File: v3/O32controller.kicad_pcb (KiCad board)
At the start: 4 copper layers, 27 x 27 mm, 125 parts, among them J1 BATT+, J10 Motor Connection, J11 Motor Connection, J12 Motor Connection, J2 BATT+, J3 BATT-, J4 BATT-, J5 NTC, J6 SWD, J7 ExternalSPI, J8 RS485, J9 RS485, Q1 CSD88584Q5DC, Q2 CSD88584Q5DC, Q3 CSD88584Q5DC, U1 STSPIN32F0ATR, U2 THVD1420DRLR, U3 MA702GQ-P

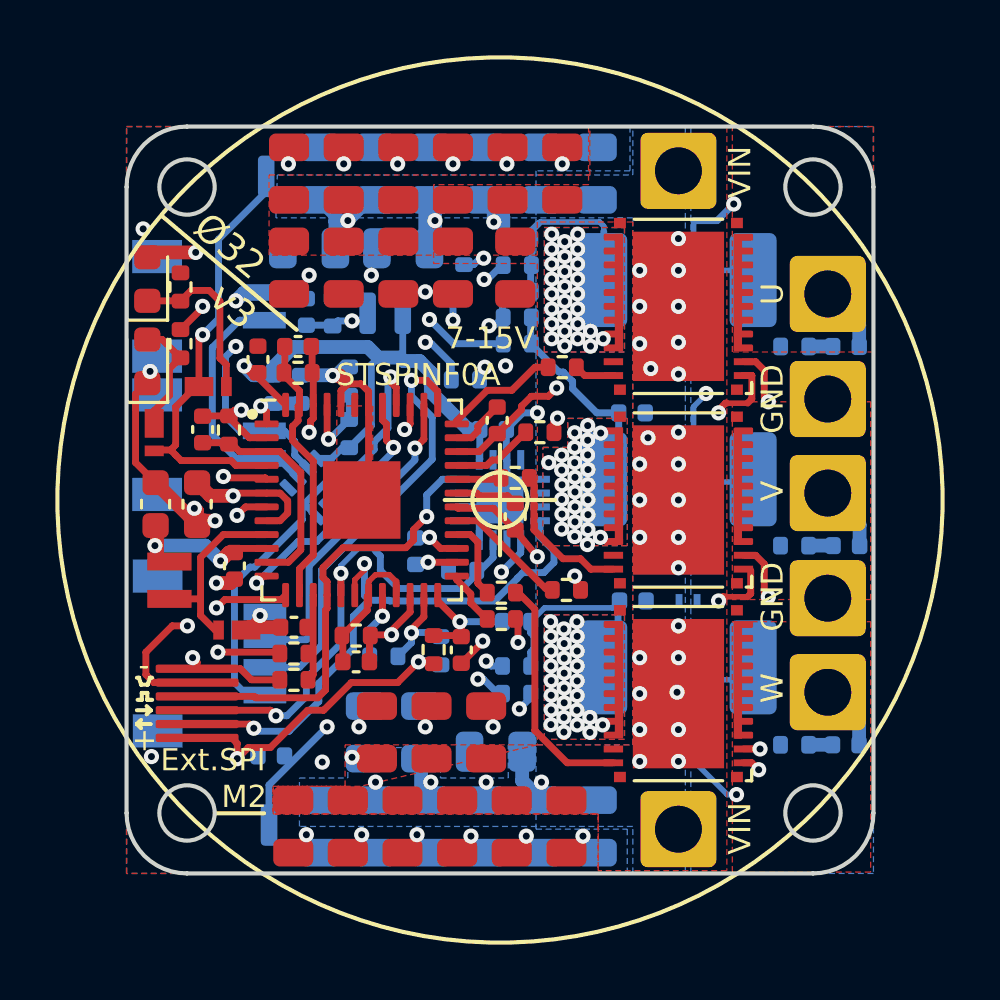
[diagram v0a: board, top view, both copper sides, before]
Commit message: use MA732 instead of 702, SMF15A
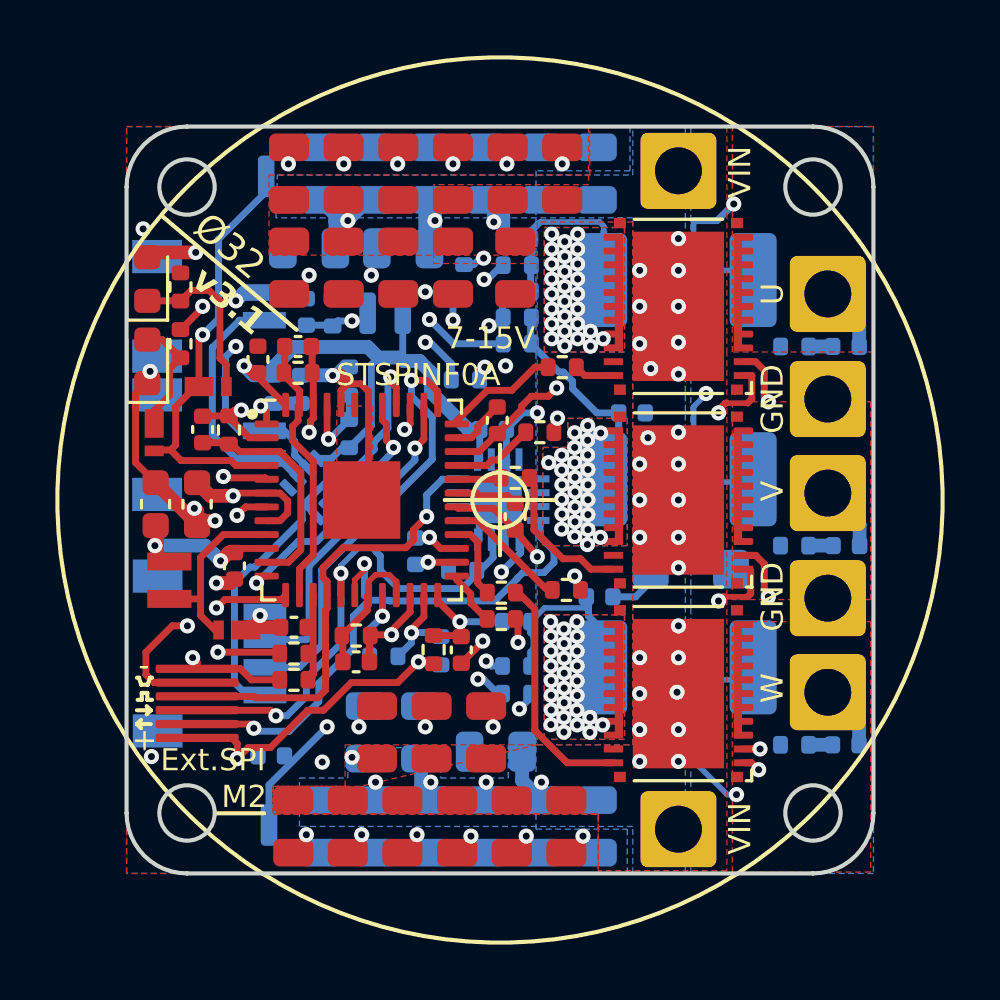
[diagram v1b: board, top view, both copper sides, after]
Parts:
- removed D2: ESDA17P20-1F2, O32controller:SMT2_0P91X0P63_STM-L
- added D7: SMF15A, Diode_SMD:D_SMF, B.Cu at (56.9, 52.5)
- U3: value MA702GQ-P -> MA732GQ-Z; footprint O32controller:MA702GQ-P -> O32controller:QFN-16_MA732
- moved C18 1.21 mm to (53.6, 53.5)
- moved U3 0.06 mm to (49.9, 50.0)
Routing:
- net VBUS: track 42.0 -> 44.1 mm
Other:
- board text added: "[07/29/24]"
- board text added: "v3.1"
- board text removed: "[12/27/23]"
- board text removed: "v3"

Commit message: finalize BOM for v3.1, shared w Axlab
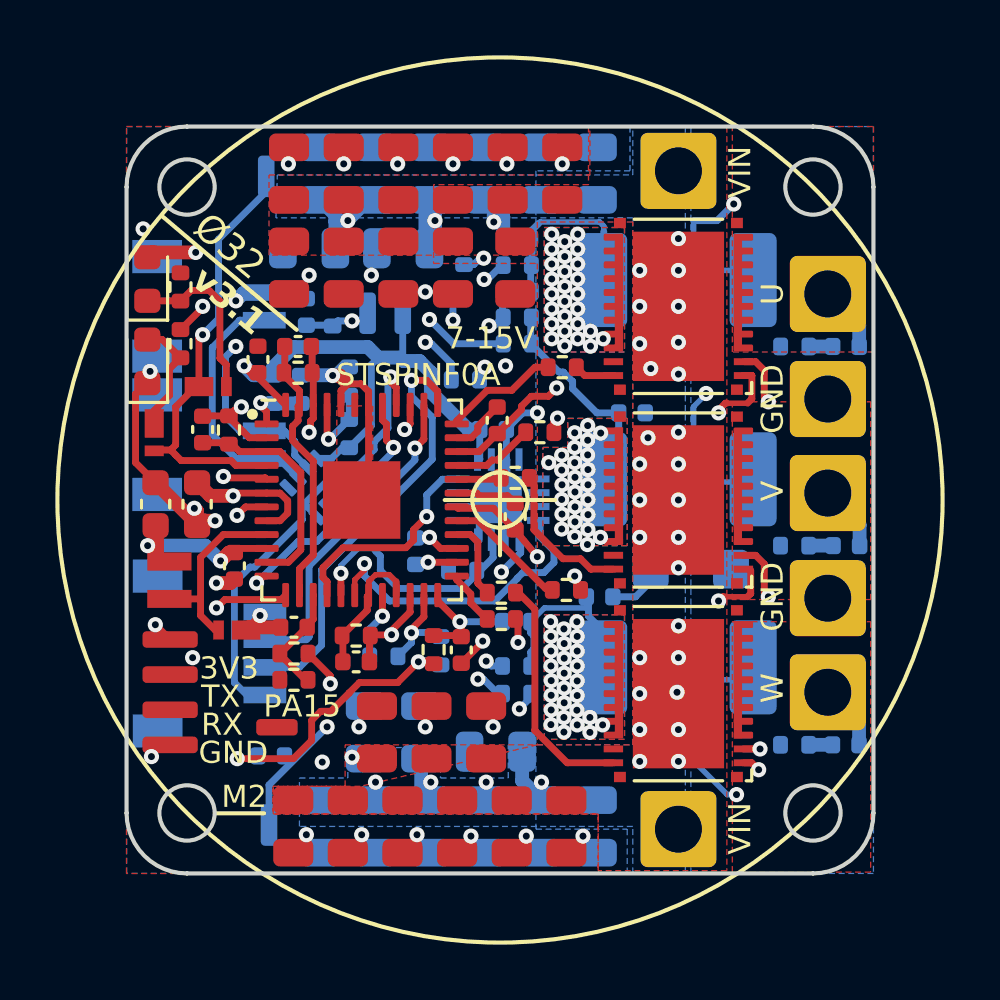
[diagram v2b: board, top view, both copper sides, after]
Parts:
- added J13: PA15, O32controller:SolderPad1-1.27mm, F.Cu at (41.9, 58.2)
- J7: value ExternalSPI -> AuxUART; footprint O32controller:FFC_0.5mm_6p -> O32controller:SolderUART-1.27mm
- moved J7 1.44 mm to (38.1, 55.0)
- turned R8 to 180 degrees
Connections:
- J7 pad 1: GND -> +3.3V
- J7 pad 2: /~{MAG2_CS} -> USART_TX
- J7 pad 3: /SPI_SCLK -> /USART_RX
- J7 pad 4: /SPI_MISO -> GND
- U1 pad 39: /~{MAG2_CS} -> /PA15
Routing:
- net /PA15: track 0.00 -> 23.0 mm, vias 0 -> 1
- net /~{MAG2_CS}: track 20.5 -> 0.00 mm, vias 2 -> 0
- net /USART_RX: track 3.99 -> 14.8 mm
- net /SPI_MOSI: track 21.1 -> 11.3 mm, vias 2 -> 1
- net /SPI_MISO: track 18.1 -> 8.83 mm, vias 2 -> 1
- net /SPI_SCLK: track 16.2 -> 8.00 mm
- net VBUS: track 44.1 -> 39.3 mm
- net GND: track 38.7 -> 34.9 mm
- net /NTC_IN: track 23.4 -> 20.7 mm
- net /BUS_SENSE: track 3.14 -> 4.06 mm
- net +3.3V: track 64.2 -> 64.3 mm, vias 7 -> 8
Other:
- board text added: "3V3"
- board text added: "MA732"
- board text added: "PA15"
- board text added: "RX"
- board text removed: "+"
- board text removed: "-"
- board text removed: "Ext.SPI"
- board text removed: "MA702"

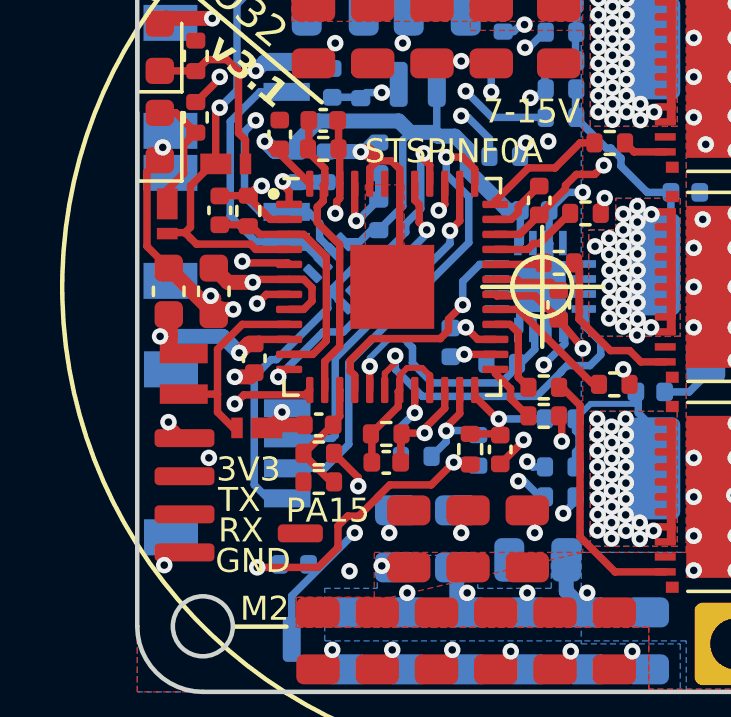
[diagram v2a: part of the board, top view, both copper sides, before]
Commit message: v3.1 design done, replaced aux spi with uart and 1 gpio, bigger TVS, and MA732
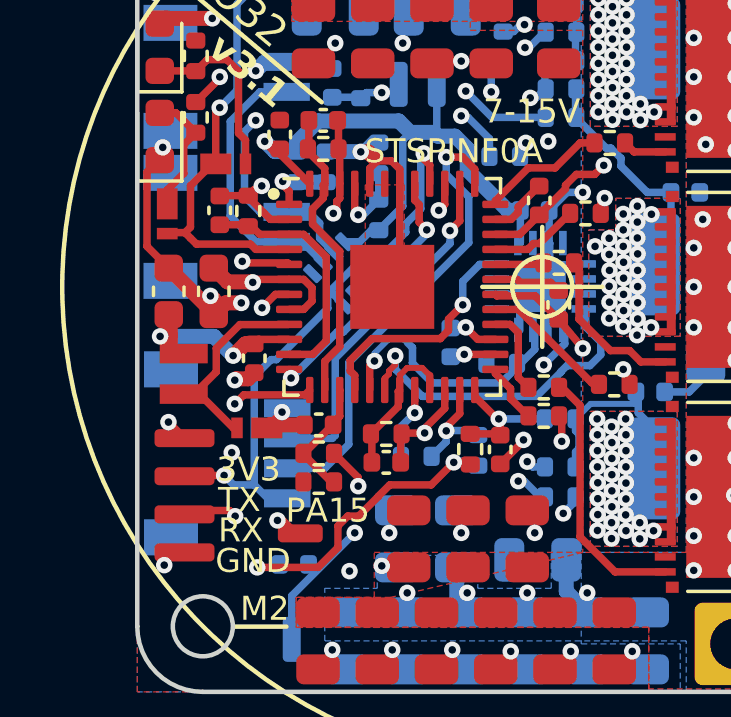
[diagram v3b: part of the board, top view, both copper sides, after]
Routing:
- net /USART_RX: track 14.8 -> 27.4 mm, vias 1 -> 2
- net USART_TX: track 17.3 -> 19.3 mm, vias 1 -> 2
- net VBUS: track 39.3 -> 37.7 mm
- net /~{MAG1_CS}: track 23.2 -> 22.2 mm
- net /USART_DE: track 5.38 -> 4.82 mm
- net /PA15: track 23.0 -> 22.7 mm, vias 1 -> 2
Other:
- board text added: "[08/09/24]"
- board text removed: "[07/29/24]"
